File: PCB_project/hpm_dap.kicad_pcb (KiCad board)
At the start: 2 copper layers, 28 x 17 mm, 50 parts, among them J1 USB_C_Receptacle_USB2.0_16P, J2 302-S101, SW1 SW_Push, U1 HPM5301IEGx, U2 TPS82130, X1 24MHz

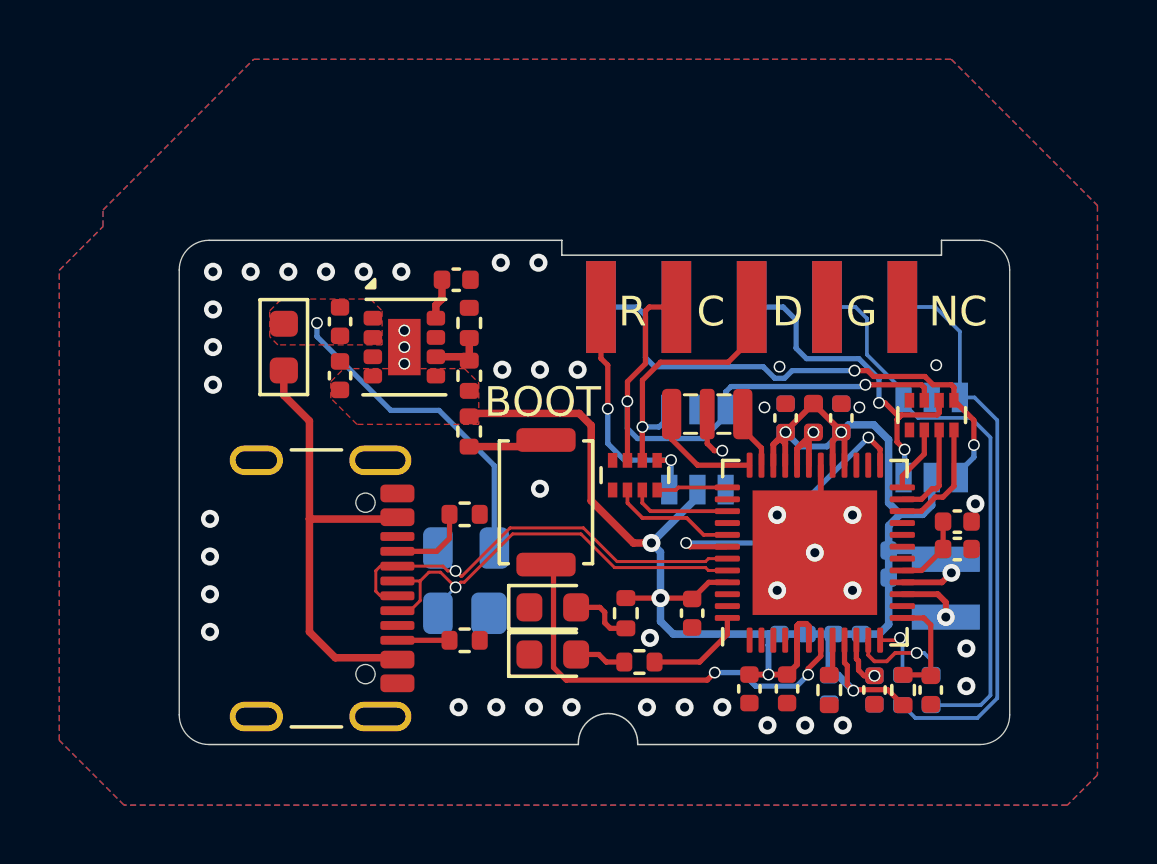
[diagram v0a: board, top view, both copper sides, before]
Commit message: 原理图错误，HPM5301的VDD_SOC引脚应当连接到内部DCDC_LP(输出)，不应当连接到3.3V供电
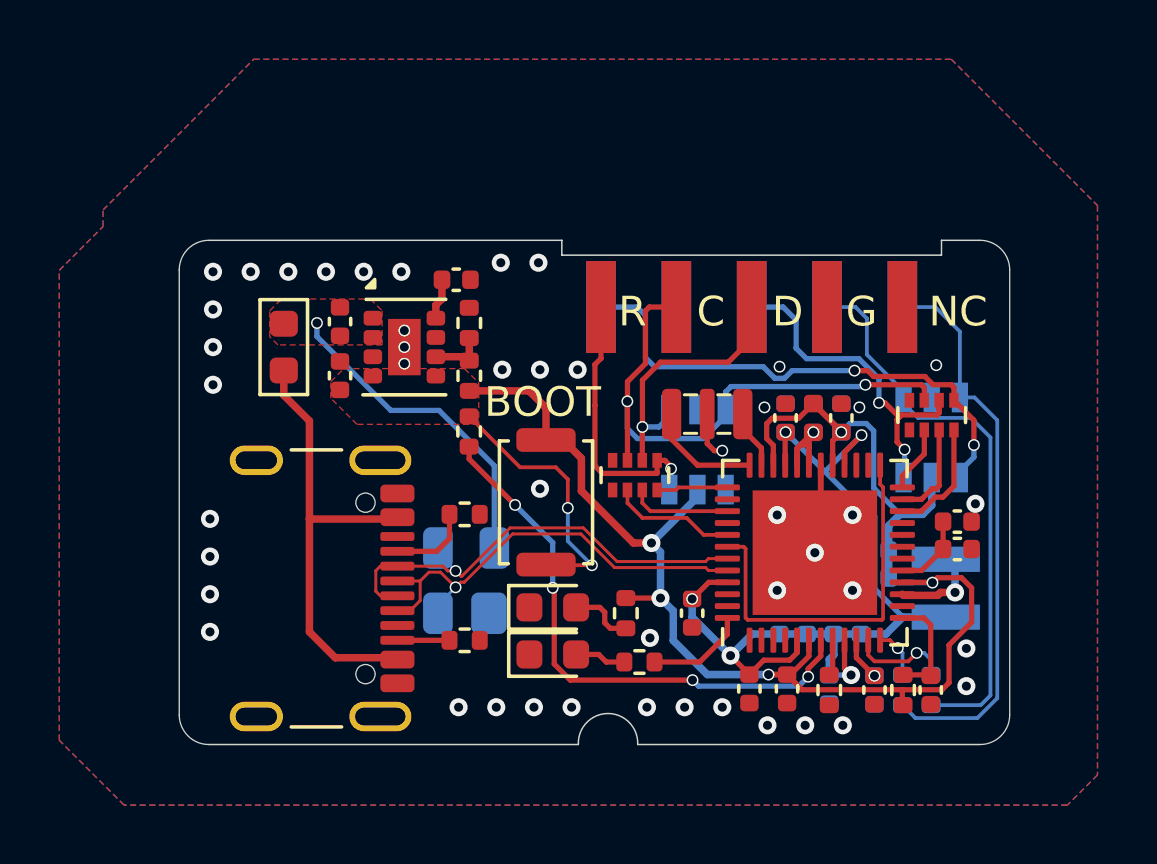
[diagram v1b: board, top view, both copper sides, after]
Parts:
- C23: moved to B.Cu
- C5: moved to F.Cu
- moved C23 1.88 mm to (75.1, 29.9)
- moved C5 1.88 mm to (73.3, 29.9)
- turned L2 to 90 degrees
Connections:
- C10 pad 1: +3.3V -> Net-(C10-Pad1)
- C11 pad 1: +3.3V -> Net-(C10-Pad1)
- C3 pad 1: +3.3V -> Net-(C10-Pad1)
- C4 pad 1: +3.3V -> Net-(C10-Pad1)
- C5 pad 1: +3.3V -> Net-(C10-Pad1)
- C6 pad 1: +3.3V -> Net-(C10-Pad1)
- C7 pad 1: +3.3V -> Net-(C10-Pad1)
- C8 pad 1: +3.3V -> Net-(C10-Pad1)
- C9 pad 1: +3.3V -> Net-(C10-Pad1)
- L2 pad 1: +3.3V -> Net-(C10-Pad1)
- R5 pad 1: +3.3V -> Net-(R5-Pad1)
- R5 pad 2: Net-(R5-Pad2) -> /core/BOOT1
- SW1 pad 1: Net-(R5-Pad2) -> +3.3V
- SW1 pad 2: /core/BOOT1 -> Net-(R5-Pad1)
- U1 pad 28: +3.3V -> Net-(C10-Pad1)
- U1 pad 33: +3.3V -> Net-(C10-Pad1)
- U1 pad 45: +3.3V -> Net-(C10-Pad1)
- U1 pad 5: +3.3V -> Net-(C10-Pad1)
- U1 pad 9: +3.3V -> Net-(C10-Pad1)
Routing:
- net Net-(C10-Pad1): track 0.00 -> 30.4 mm, vias 0 -> 5
- net +3.3V: track 63.6 -> 51.4 mm, vias 7 -> 5
- net Net-(R5-Pad1): track 0.00 -> 8.91 mm, vias 0 -> 2
- net /core/BOOT1: track 14.2 -> 18.9 mm, vias 2 -> 4
- net Net-(R5-Pad2): track 2.68 -> 0.00 mm
- net /core/SPI_CS: track 10.6 -> 12.9 mm, vias 2 -> 0
- net Net-(U1A-DCDC_LP): track 2.08 -> 3.08 mm
- net /SWRST/JTAG_TRST: track 8.55 -> 9.43 mm, vias 2 -> 1
